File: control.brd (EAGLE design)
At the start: 186 x 186 mm, 103 parts, among them CN1 40PIN FPC, CN2 MINI B USB, CN3 2X10 HEADER, CN4 2X10 HEADER, SW1 TACT, SW10 TACT, SW11 TACT, SW12 TACT, SW13 TACT, SW14 TACT, SW15 TACT, SW16 TACT, SW2 TACT, SW3 TACT, SW4 TACT, SW5 TACT, SW6 TACT, SW7 TACT, SW8 TACT, SW9 TACT, U1 STM32H743ZI, U2 AS4C8M16SA, U3 TPS61169DCKR, U4 USBLC6-2SC6, U5 FT230X, U6 DCDC 3V3

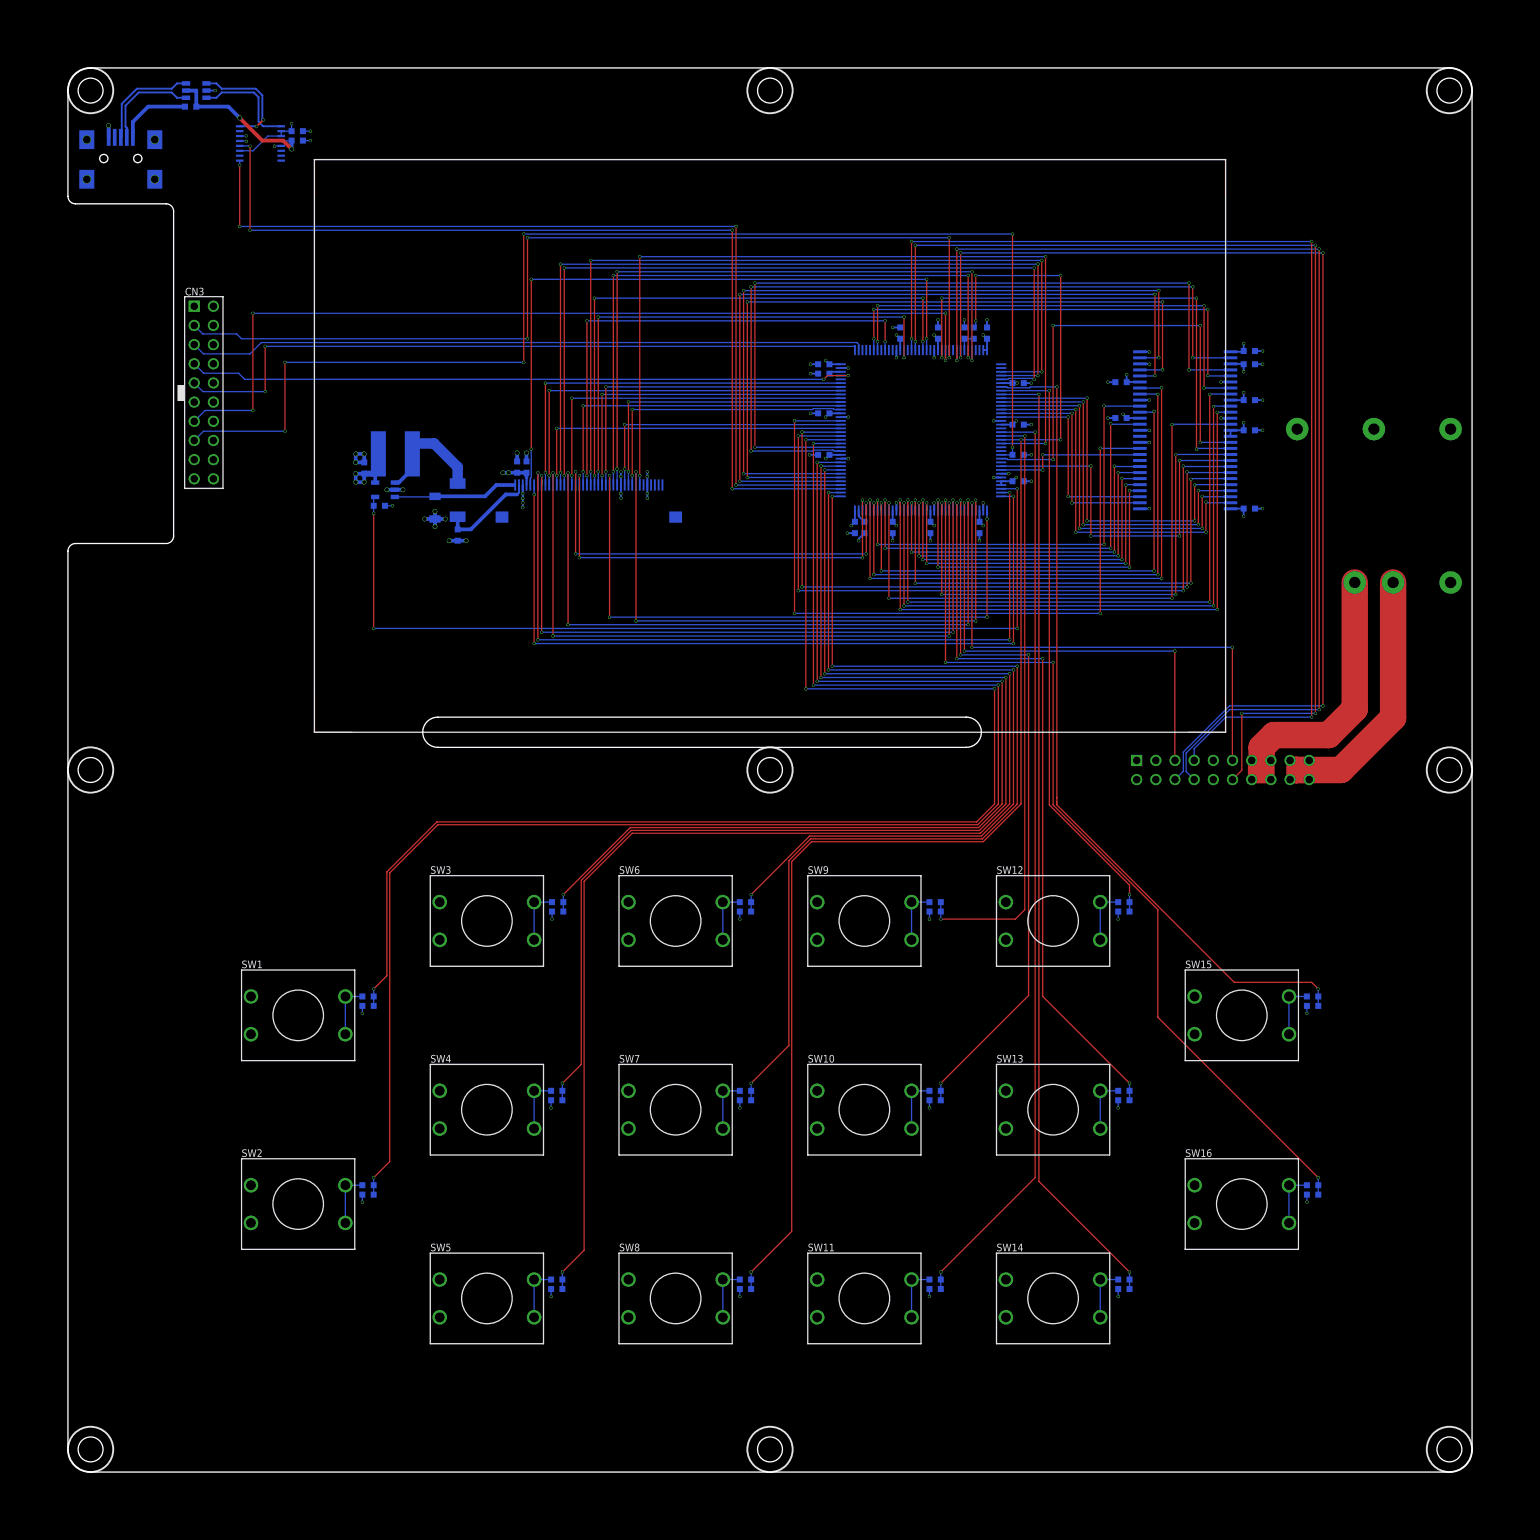
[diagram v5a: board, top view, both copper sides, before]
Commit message: DRC passes on both PCBs, pushed to Fusion
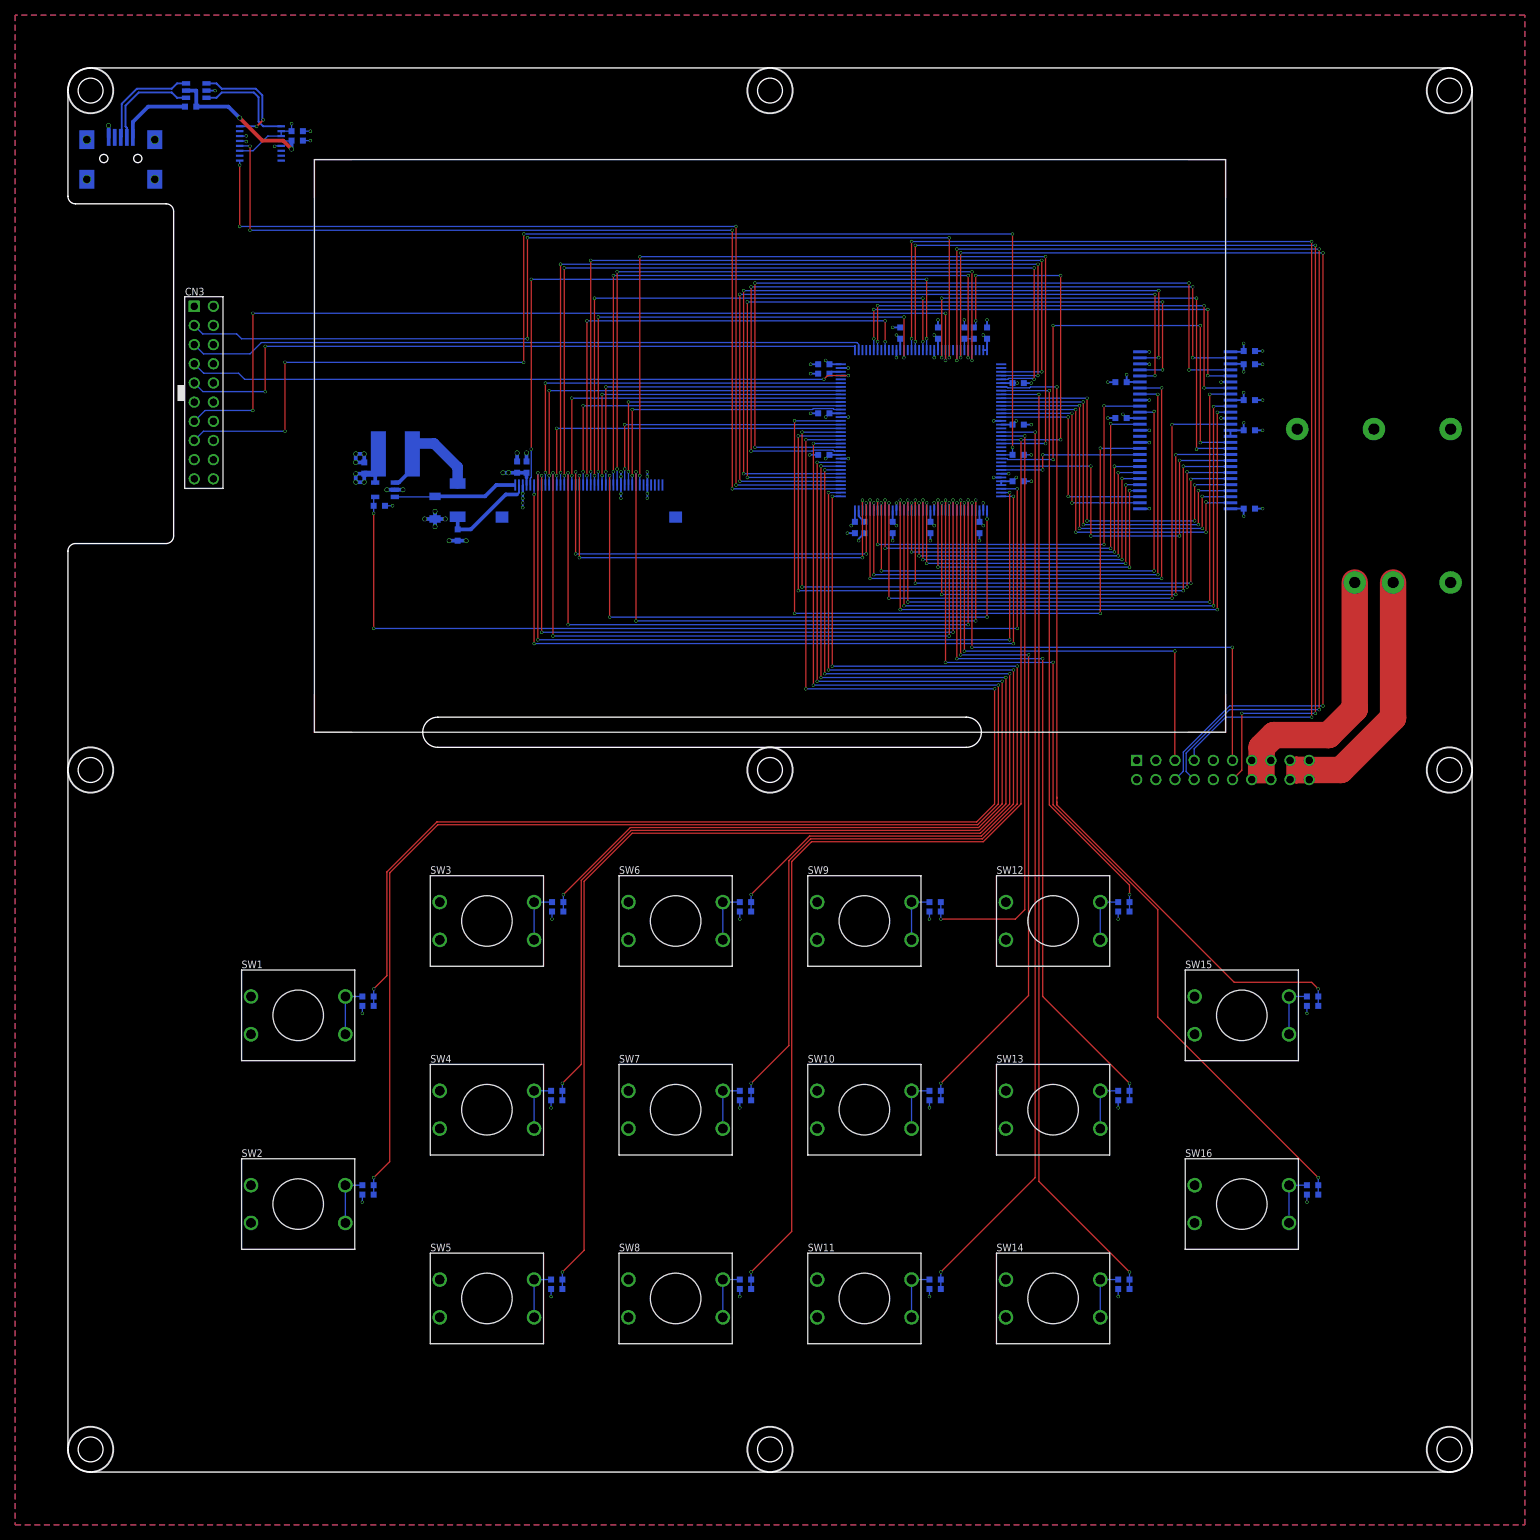
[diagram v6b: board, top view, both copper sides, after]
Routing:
- net SDRAM_BA0: track 100.4 -> 99.9 mm
- added copper zone on layer 1, net GND
- added copper zone on layer 16, net GND
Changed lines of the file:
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@@
 <setting verticaltext="up"/>
 </settings>
-<grid distance="0.125" unitdist="mm" unit="mm" style="lines" multiple="1" display="yes" altdistance="0.125" altunitdist="mm" altunit="mm"/>
+<grid distance="0.25" unitdist="mm" unit="mm" style="lines" multiple="1" display="yes" altdistance="0.125" altunitdist="mm" altunit="mm"/>
 <layers>
 <layer number="1" name="Top" color="4" fill="1" visible="yes" active="yes"/>
@@
 </layers>
 <board>
-<fusionsync huburn="a.cGVyc29uYWw6dWUyYjllNWFm" projecturn="a.cGVyc29uYWw6dWUyYjllNWFmIzIwMjAwODI1MzI2NDUzNDMx" f3durn="urn:adsk.wipprod:dm.lineage:wnPGf6KyQv68ik76HDulcw" pcbguid="" lastpulledtime="" lastsyncedchangeguid="" latestrevisionid="093d7112-a247-4842-ac6e-0f58440f59c5" lastsyncedrevisionid="093d7112-a247-4842-ac6e-0f58440f59c5" lastboardhashguid="5ccaa559-bc30-ebaf-a50a-9b2d6f7c8b86" lastpushedtime="2020-10-08T15:31:04Z" linktopcb3d="true"/>
+<fusionsync huburn="a.cGVyc29uYWw6dWUyYjllNWFm" projecturn="a.cGVyc29uYWw6dWUyYjllNWFmIzIwMjAwODI1MzI2NDUzNDMx" f3durn="urn:adsk.wipprod:dm.lineage:wnPGf6KyQv68ik76HDulcw" pcbguid="" lastpulledtime="" lastsyncedchangeguid="" latestrevisionid="b66c71c2-44e7-437f-ba9f-58cd7608af97" lastsyncedrevisionid="b66c71c2-44e7-437f-ba9f-58cd7608af97" lastboardhashguid="42ca8785-fddb-a2be-0827-848ff4e22217" lastpushedtime="2020-10-08T18:08:47Z" linktopcb3d="true"/>
 <plain>
 <wire x1="90" y1="-93" x2="93" y2="-90" width="0" layer="20" curve="90" locked="yes"/>
@@
 <contactref element="CN3" pad="18"/>
 <contactref element="CN3" pad="6"/>
+<polygon width="0.15" layer="1">
+<vertex x="-100" y="-100"/>
+<vertex x="100" y="-100"/>
+<vertex x="100" y="100"/>
+<vertex x="-100" y="100"/>
+</polygon>
+<polygon width="0.15" layer="16">
+<vertex x="-100" y="-100"/>
+<vertex x="100" y="-100"/>
+<vertex x="100" y="100"/>
+<vertex x="-100" y="100"/>
+</polygon>
 </signal>
 <signal name="3V3">
@@
 <wire x1="58.3" y1="49.8" x2="58.25" y2="49.75" width="0.15" layer="16"/>
 <via x="58.25" y="49.75" extent="1-16" drill="0.3"/>
-<wire x1="58.25" y1="22.25" x2="58.25" y2="22.375" width="0.15" layer="1"/>
 <via x="58.25" y="22.25" extent="1-16" drill="0.3"/>
 <wire x1="58.25" y1="49.75" x2="58.25" y2="22.25" width="0.15" layer="1"/>
@@
 <via x="3.75" y="44.25" extent="1-16" drill="0.3"/>
 <wire x1="3.75" y1="44.25" x2="9.375" y2="44.25" width="0.15" layer="16"/>
-<wire x1="9.375" y1="44.25" x2="9.875" y2="44.25" width="0.15" layer="16"/>
 </signal>
 <signal name="SDRAM_A11">

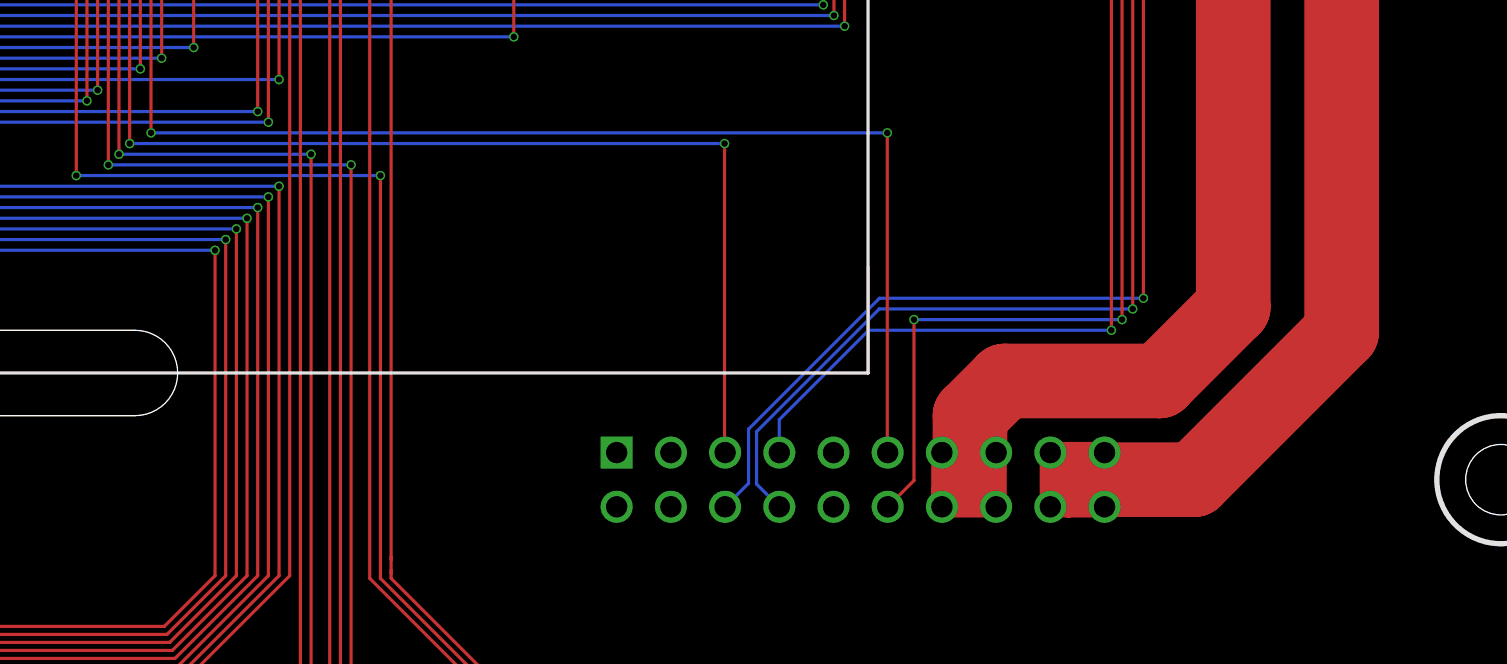
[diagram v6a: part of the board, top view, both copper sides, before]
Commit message: Bridge connector fixed
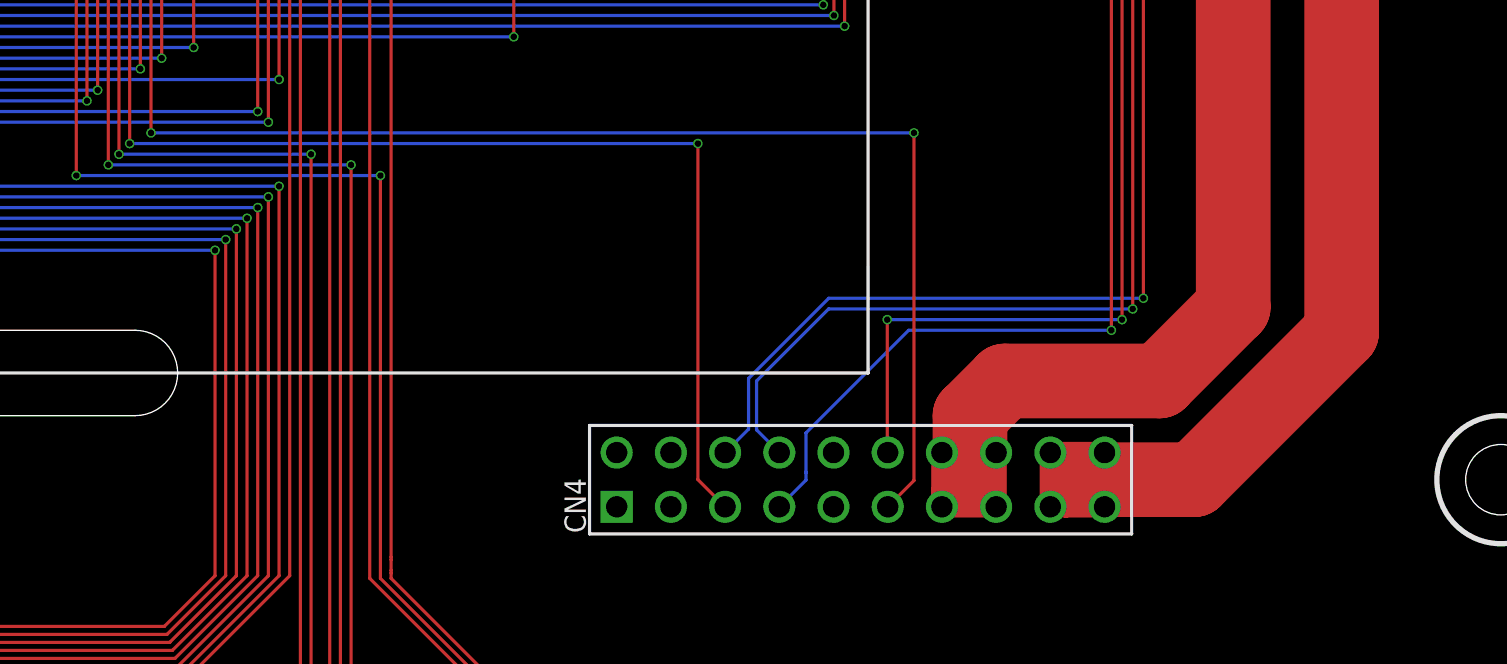
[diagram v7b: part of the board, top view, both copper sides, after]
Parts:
- flipped CN4 to the top, turned to 90 degrees
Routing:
- net ADC_SPI_SCLK: track 69.6 -> 73.9 mm
- net ADC_SPI_MOSI: track 63.0 -> 64.8 mm
- net ADC_SPI_!CS: track 147.9 -> 146.1 mm
- net ADC_SPI_MISO: track 149.2 -> 150.7 mm
- net DAC_I2C_SCL: track 149.1 -> 147.9 mm
- net DAC_I2C_SDA: track 148.0 -> 146.9 mm

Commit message: Checked against Cube
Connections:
- removed net N$104: U1.135
- removed net N$125: U1.111
- removed net N$126: U1.112
- removed net N$127: U1.113
- removed net N$133: U1.116
- removed net N$135: U1.118
- removed net N$136: U1.119
- removed net N$138: U1.123
- removed net N$161: U1.142
- removed net N$162: U1.141
- removed net N$180: U1.129
- removed net N$183: U1.126
- removed net N$4: U1.18
- removed net N$5: U1.1
- removed net N$6: U1.2
- removed net N$84: U1.27
- removed net N$95: U1.104
- net ADC_!DRDY: now also U1.27
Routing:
- net ADC_!DRDY: track 0.00 -> 74.6 mm, vias 0 -> 3
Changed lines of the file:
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@@
 </layers>
 <board>
-<fusionsync huburn="a.cGVyc29uYWw6dWUyYjllNWFm" projecturn="a.cGVyc29uYWw6dWUyYjllNWFmIzIwMjAwODI1MzI2NDUzNDMx" f3durn="urn:adsk.wipprod:dm.lineage:wnPGf6KyQv68ik76HDulcw" pcbguid="" lastpulledtime="" lastsyncedchangeguid="" latestrevisionid="ca8c3dbd-8e61-403d-8a57-4038a2737acd" lastsyncedrevisionid="ca8c3dbd-8e61-403d-8a57-4038a2737acd" lastboardhashguid="a41f287c-54a8-c81c-84c3-8a668f3cb690" lastpushedtime="2020-10-08T18:21:52Z" linktopcb3d="true"/>
+<fusionsync huburn="a.cGVyc29uYWw6dWUyYjllNWFm" projecturn="a.cGVyc29uYWw6dWUyYjllNWFmIzIwMjAwODI1MzI2NDUzNDMx" f3durn="urn:adsk.wipprod:dm.lineage:wnPGf6KyQv68ik76HDulcw" pcbguid="" lastpulledtime="" lastsyncedchangeguid="" latestrevisionid="06f15686-0416-4ee5-bf46-efffa6f91c55" lastsyncedrevisionid="06f15686-0416-4ee5-bf46-efffa6f91c55" lastboardhashguid="fab530b9-1610-bf14-5bc2-751c0d396012" lastpushedtime="2020-10-08T19:35:29Z" linktopcb3d="true"/>
 <plain>
 <wire x1="90" y1="-93" x2="93" y2="-90" width="0" layer="20" curve="90" locked="yes"/>
@@
 <wire x1="52.375" y1="0.005" x2="52.375" y2="15.75" width="0.15" layer="1"/>
 </signal>
-<signal name="N$95">
-<contactref element="U1" pad="104"/>
-</signal>
 <signal name="JTAG_TMS">
 <contactref element="U1" pad="105"/>
@@
 <wire x1="-32.125" y1="57.125" x2="-70.005" y2="57.125" width="0.15" layer="16"/>
 </signal>
-<signal name="N$104">
-<contactref element="U1" pad="135"/>
-</signal>
 <signal name="DAC_I2C_SCL">
 <contactref element="U1" pad="136"/>
@@
 <wire x1="57" y1="58.875" x2="37.5" y2="58.875" width="0.15" layer="16"/>
 <via x="37.5" y="58.875" extent="1-16" drill="0.3"/>
-<wire x1="37.5" y1="58.875" x2="37.5" y2="41.125" width="0.15" layer="1"/>
-<via x="37.5" y="41.125" extent="1-16" drill="0.3"/>
-<wire x1="37.5" y1="41.125" x2="31.5" y2="41.125" width="0.15" layer="16"/>
+<wire x1="37.5" y1="58.875" x2="37.5" y2="41.25" width="0.15" layer="1"/>
+<via x="37.5" y="41.25" extent="1-16" drill="0.3"/>
+<wire x1="34.25" y1="41.125" x2="31.5" y2="41.125" width="0.15" layer="16"/>
 <wire x1="31.5" y1="41.125" x2="31.375" y2="41.25" width="0.15" layer="16"/>
 <wire x1="31.375" y1="41.25" x2="30.625" y2="41.25" width="0.15" layer="16"/>
+<wire x1="37.5" y1="41.25" x2="34.375" y2="41.25" width="0.15" layer="16"/>
+<wire x1="34.375" y1="41.25" x2="34.25" y2="41.125" width="0.15" layer="16"/>
 </signal>
 <signal name="SDRAM_!CS">
@@
 <via x="-18.75" y="39.5" extent="1-16" drill="0.3"/>
 <wire x1="-18.75" y1="39.5" x2="-18.75" y2="37.75" width="0.15" layer="16"/>
-</signal>
-<signal name="N$125">
-<contactref element="U1" pad="111"/>
-</signal>
-<signal name="N$126">
-<contactref element="U1" pad="112"/>
-</signal>
-<signal name="N$127">
-<contactref element="U1" pad="113"/>
 </signal>
 <signal name="SDRAM_D2">
@@
 <wire x1="14.25" y1="56.75" x2="14.25" y2="55.625" width="0.15" layer="16"/>
 <wire x1="57.5" y1="61.5" x2="14.25" y2="61.5" width="0.15" layer="16"/>
-</signal>
-<signal name="N$133">
-<contactref element="U1" pad="116"/>
-</signal>
-<signal name="N$135">
-<contactref element="U1" pad="118"/>
-</signal>
-<signal name="N$136">
-<contactref element="U1" pad="119"/>
-</signal>
-<signal name="N$138">
-<contactref element="U1" pad="123"/>
 </signal>
 <signal name="SDRAM_D13">
@@
 <wire x1="18.25" y1="35.75" x2="18.25" y2="22.25" width="0.15" layer="1"/>
 </signal>
-<signal name="N$161">
-<contactref element="U1" pad="142"/>
-</signal>
-<signal name="N$162">
-<contactref element="U1" pad="141"/>
-</signal>
 <signal name="SDRAM_A9">
 <contactref element="U1" pad="55"/>
@@
 <via x="22.75" y="54.625" extent="1-16" drill="0.3"/>
 <wire x1="22.75" y1="54.625" x2="22.75" y2="55.625" width="0.15" layer="16"/>
-</signal>
-<signal name="N$180">
-<contactref element="U1" pad="129"/>
-</signal>
-<signal name="N$183">
-<contactref element="U1" pad="126"/>
 </signal>
 <signal name="ADC_SPI_!CS">
@@
 <wire x1="19.25" y1="35.75" x2="19.25" y2="34.375" width="0.15" layer="16"/>
 </signal>
-<signal name="N$84">
-<contactref element="U1" pad="27"/>
-</signal>
 <signal name="DISP_PWM">
 <contactref element="U3" pad="4"/>
@@
 <signal name="ADC_!DRDY">
 <contactref element="CN4" pad="5"/>
+<contactref element="U1" pad="27"/>
+<wire x1="30.625" y1="40.75" x2="38.5" y2="40.75" width="0.15" layer="16"/>
+<via x="38.5" y="40.75" extent="1-16" drill="0.3"/>
+<wire x1="38.5" y1="40.75" x2="38.5" y2="-3.5" width="0.15" layer="1"/>
+<via x="38.5" y="-3.5" extent="1-16" drill="0.3"/>
+<wire x1="38.5" y1="-3.5" x2="58.75" y2="-3.5" width="0.15" layer="16"/>
+<via x="58.75" y="-3.5" extent="1-16" drill="0.3"/>
+<wire x1="58.75" y1="-3.5" x2="58.75" y2="-1.29" width="0.15" layer="1"/>
+<wire x1="58.75" y1="-1.29" x2="58.73" y2="-1.27" width="0.15" layer="1"/>
 </signal>
 <signal name="PGND">
@@
 <wire x1="65.58" y1="-0.5" x2="63.81" y2="-0.5" width="1" layer="1"/>
 </signal>
-<signal name="N$4">
-<contactref element="U1" pad="18"/>
-</signal>
-<signal name="N$5">
-<contactref element="U1" pad="1"/>
-</signal>
-<signal name="N$6">
-<contactref element="U1" pad="2"/>
-</signal>
 </signals>
